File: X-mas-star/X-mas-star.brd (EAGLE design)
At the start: 95.7 x 91 mm, 7 parts

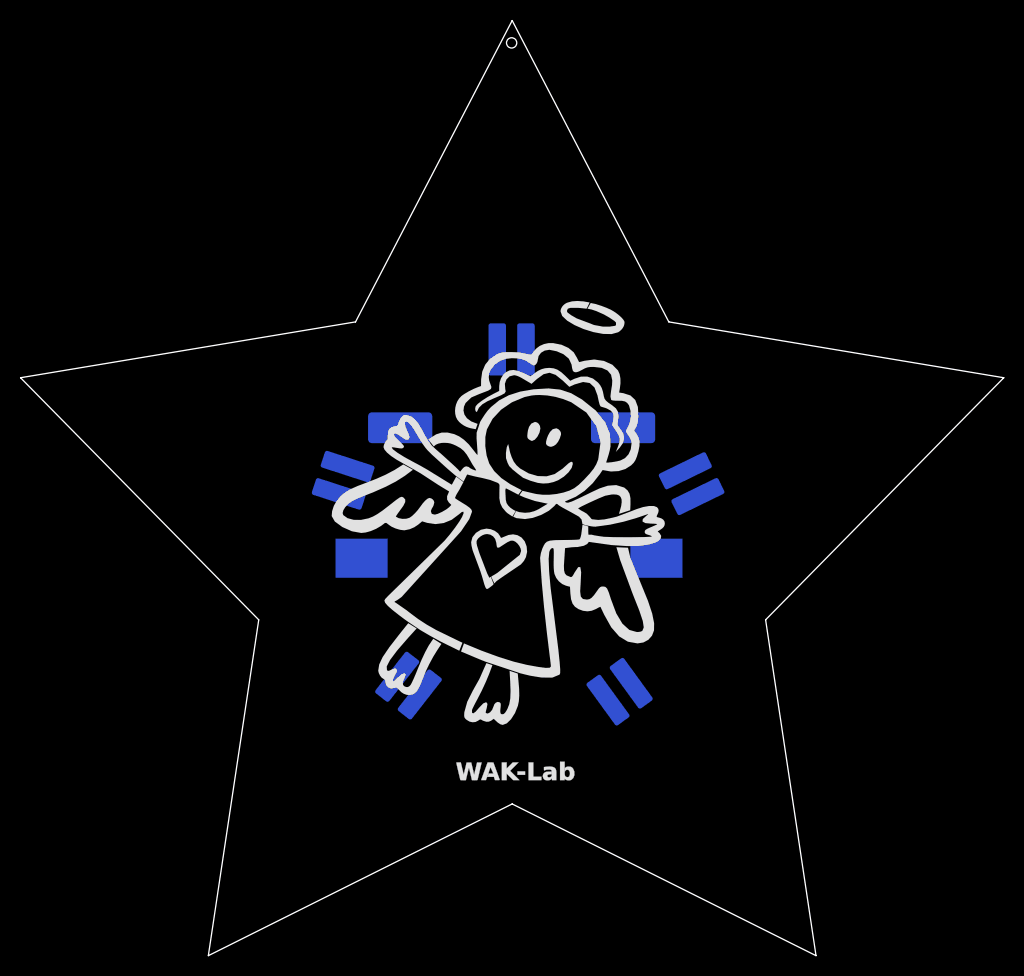
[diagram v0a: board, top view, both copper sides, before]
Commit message: Copper Background
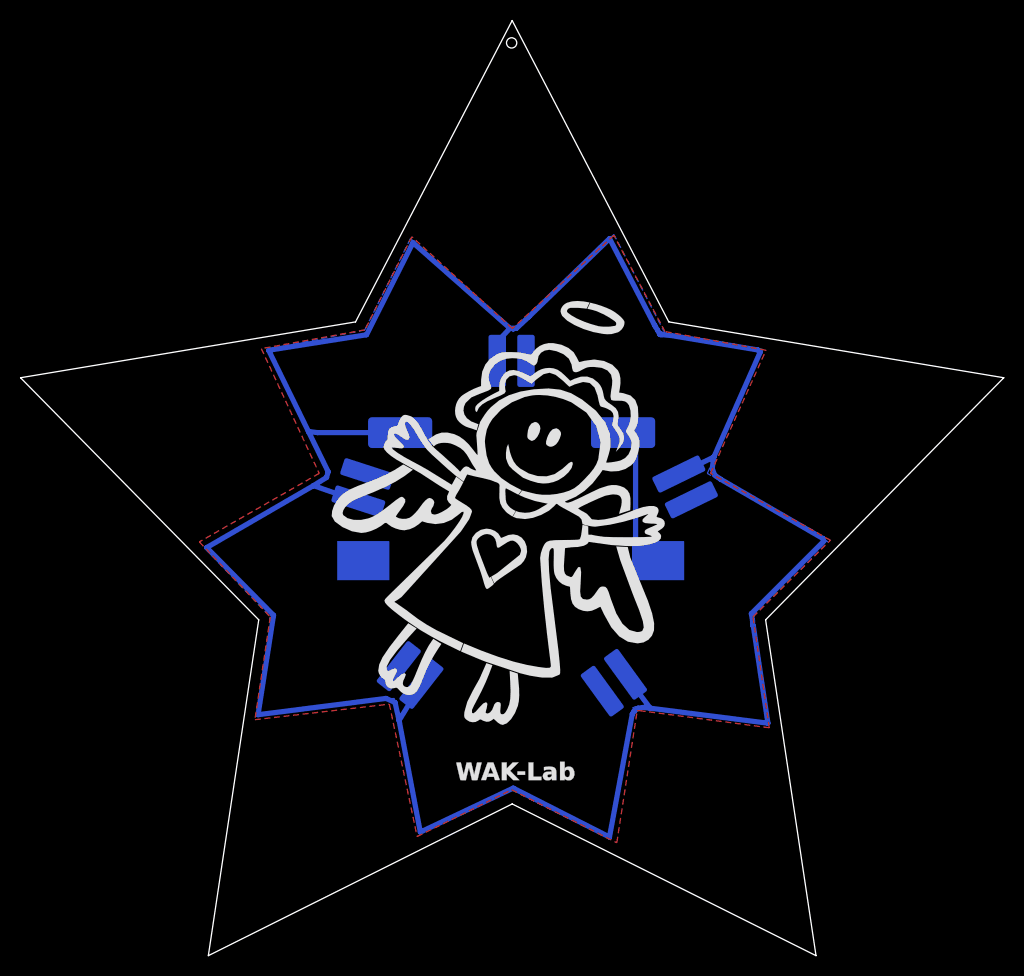
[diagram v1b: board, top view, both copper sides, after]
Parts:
- moved D4 2.03 mm to (26.6, 49.6)
- moved D3 1.11 mm to (43.5, 63.7)
- moved D5 1.04 mm to (32.0, 28.5)
- moved D2 1.03 mm to (54.9, 27.7)
- moved D1 0.71 mm to (62.7, 50.0)
- moved S1 0.48 mm to (43.5, 54.1)
- moved G1 0.29 mm to (43.3, 41.7)
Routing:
- net N$12: track 0.00 -> 260.8 mm
- net N$29: track 0.00 -> 18.2 mm
- added copper zone on layer 16, net GND
- added copper zone on layer 1, net GND1
